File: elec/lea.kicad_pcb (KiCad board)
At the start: 2 copper layers, 76.2 x 76.2 mm, 9 parts, among them J1 Servomoteur, J2 Screw_Terminal_01x02, J3 Jack, SW1 SW_SPDT

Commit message: commit avant changement de branche
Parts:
- J2: moved to B.Cu
- moved SW1 43.6 mm to (101.6, 76.2), turned to -90 degrees
- moved C2 31.9 mm to (110.5, 76.2), turned to 180 degrees
- moved J3 22.5 mm to (120.6, 121.9), turned to 180 degrees
- moved J1 21.6 mm to (116.8, 76.2), turned to 0 degrees
- moved C1 21.1 mm to (148.7, 77.5), turned to -90 degrees
- moved A1 20.5 mm to (129.5, 77.5)
- moved J2 13.7 mm to (109.2, 68.6), turned to 90 degrees
- moved C3 7.74 mm to (121.8, 66.0), turned to 180 degrees
- moved D1 7.18 mm to (132.1, 68.6), turned to 0 degrees
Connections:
- J3 pad 1: GND -> /JCK
- J3 pad 2: /JCK -> GND
- SW1 pad 1: +9V -> unconnected-(SW1-Pad1)
- SW1 pad 3: unconnected-(SW1-Pad3) -> +9V
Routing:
- net /VIN: track 0.00 -> 66.4 mm
- net +9V: track 0.00 -> 48.8 mm
- net /JCK: track 0.00 -> 27.1 mm
- net /PWM: track 0.00 -> 17.2 mm
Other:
- outline, holes or cut-outs redrawn
- board text added: "33 × 25 mm"

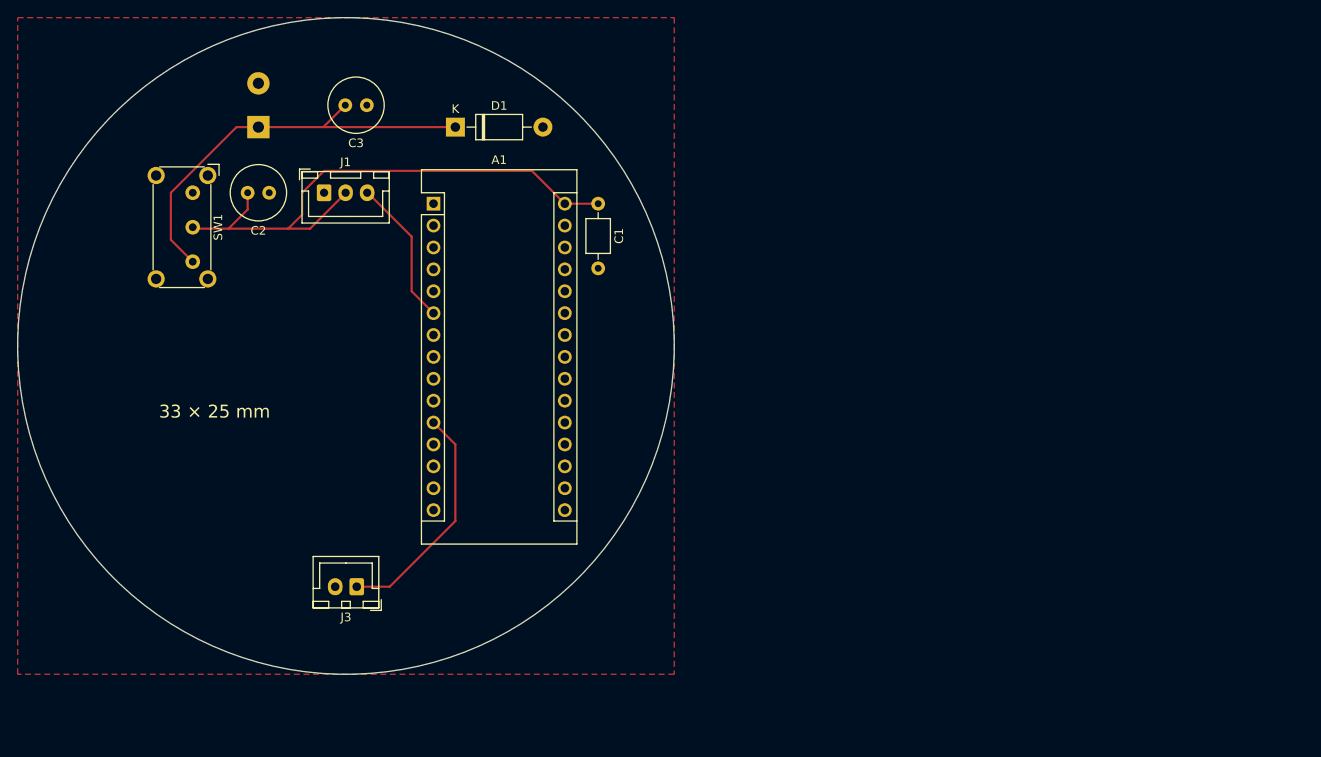
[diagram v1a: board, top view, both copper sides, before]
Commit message: Refonte complète du circuit
- réagencement des composants sur le schéma
- pcb désormais rectangulaire
- ajout du régulateur de tension et de son empreinte
- masses séparées avec possibilité de pont
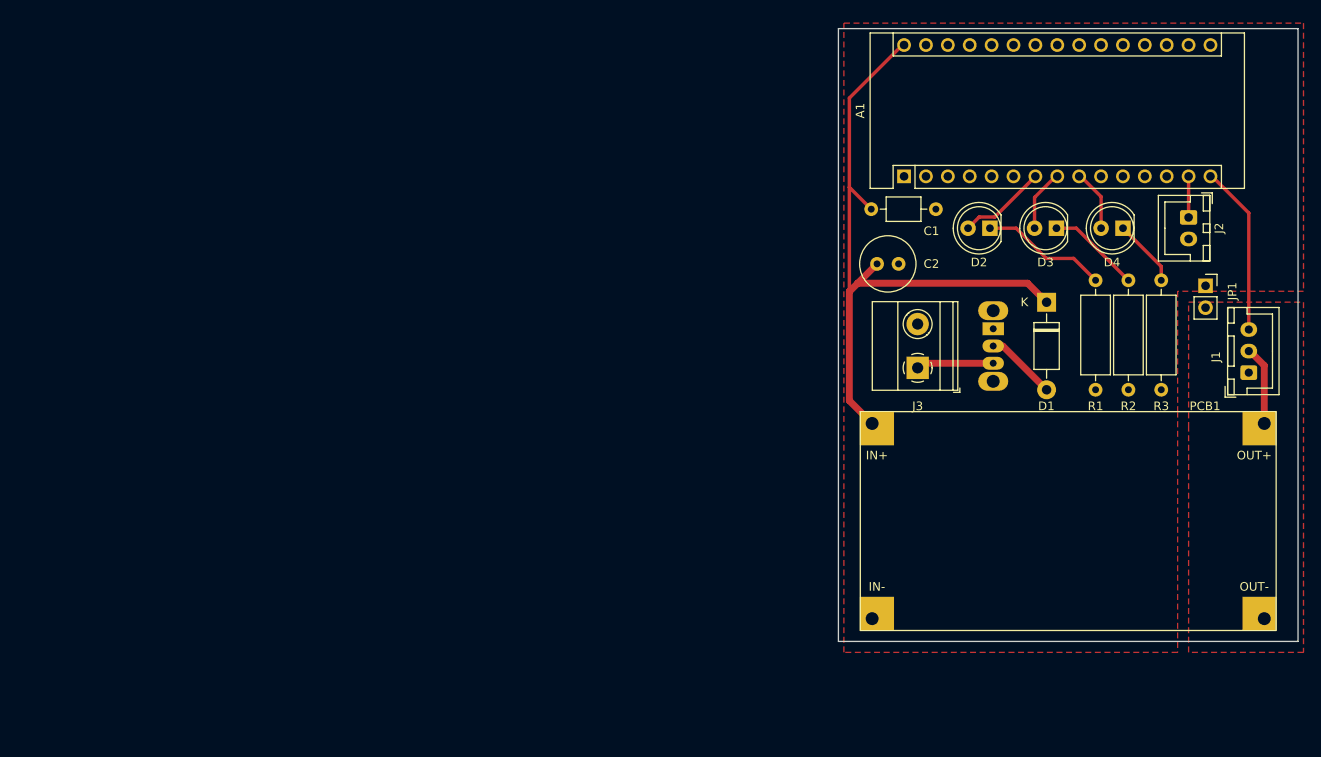
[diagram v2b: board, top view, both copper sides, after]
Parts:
- removed C3: 10uF, Capacitor_THT:C_Radial_D6.3mm_H5.0mm_P2.50mm
- added D2: LED, LED_THT:LED_D5.0mm, F.Cu at (194.1, 80.3)
- added D3: LED, LED_THT:LED_D5.0mm, F.Cu at (201.8, 80.3)
- added D4: LED, LED_THT:LED_D5.0mm, F.Cu at (209.6, 80.3)
- added JP1: Jumper_2_Open, Connector_PinSocket_2.54mm:PinSocket_1x02_P2.54mm_Vertical, F.Cu at (219.1, 87.0)
- added PCB1: abaisseur, meiVestigii:abaisseur_TOP-AERO, F.Cu at (201.9, 114.3)
- added R1: R, Resistor_THT:R_Axial_DIN0309_L9.0mm_D3.2mm_P12.70mm_Horizontal, F.Cu at (206.4, 99.1)
- added R2: R, Resistor_THT:R_Axial_DIN0309_L9.0mm_D3.2mm_P12.70mm_Horizontal, F.Cu at (210.2, 99.1)
- added R3: R, Resistor_THT:R_Axial_DIN0309_L9.0mm_D3.2mm_P12.70mm_Horizontal, F.Cu at (214.0, 99.1)
- D1: value 1N4001 -> 1N4002
- J2: value Screw_Terminal_01x02 -> Jack; footprint TerminalBlock_Phoenix:TerminalBlock_Phoenix_MKDS-1,5-2-5.08_1x02_P5.08mm_Horizontal -> Connector_JST:JST_XH_B2B-XH-A_1x02_P2.50mm_Vertical; moved to F.Cu
- J3: value Jack -> Screw_Terminal_01x02; footprint Connector_JST:JST_XH_B2B-XH-A_1x02_P2.50mm_Vertical -> TerminalBlock_Phoenix:TerminalBlock_Phoenix_MKDS-1,5-2-5.08_1x02_P5.08mm_Horizontal
- SW1: footprint Button_Switch_THT:SW_E-Switch_EG1224_SPDT_Angled -> Button_Switch_THT:SW_Slide_1P2T_CK_OS102011MS2Q; moved to B.Cu
- moved J1 109.3 mm to (224.2, 97.1), turned to 90 degrees
- moved J2 108.5 mm to (217.2, 79.1), turned to -90 degrees
- moved SW1 94.2 mm to (194.5, 92.0)
- moved C2 73.5 mm to (183.5, 84.5)
- moved D1 71.6 mm to (200.7, 88.9), turned to -90 degrees
- moved J3 69.9 mm to (185.7, 96.5), turned to 90 degrees
- moved A1 54.7 mm to (184.2, 74.3), turned to 90 degrees
- moved C1 31.7 mm to (180.3, 78.1), turned to 0 degrees
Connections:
- A1 pad 11: /JCK -> unconnected-(A1-Pad11)
- A1 pad 14: unconnected-(A1-Pad14) -> /JCK
- A1 pad 15: unconnected-(A1-Pad15) -> /PWM
- A1 pad 6: /PWM -> unconnected-(A1-Pad6)
- A1 pad 7: unconnected-(A1-Pad7) -> /D4
- A1 pad 8: unconnected-(A1-Pad8) -> /D5
- A1 pad 9: unconnected-(A1-Pad9) -> /D6
- D1 pad 1: +9V -> /VIN
- D1 pad 2: GND -> Net-(D1-Pad2)
- J1 pad 1: GND -> GND1
- J1 pad 2: /VIN -> /V1
- J2 pad 1: +9V -> /JCK
- J3 pad 1: /JCK -> +9V
- SW1 pad 2: /VIN -> Net-(D1-Pad2)
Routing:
- net +9V: track 48.8 -> 8.99 mm
- net /JCK: track 27.1 -> 4.96 mm
- net Net-(D2-Pad1): track 0.00 -> 14.8 mm
- net /VIN: track 66.4 -> 78.8 mm
- net Net-(D3-Pad1): track 0.00 -> 10.9 mm
- net /D4: track 0.00 -> 10.3 mm
- net /V1: track 0.00 -> 9.22 mm
- net Net-(D1-Pad2): track 0.00 -> 8.30 mm
- net Net-(D4-Pad1): track 0.00 -> 7.88 mm
- net /D5: track 0.00 -> 7.30 mm
- net /D6: track 0.00 -> 7.26 mm
- net /PWM: track 17.2 -> 19.8 mm
- added copper zone on F.Cu, net GND1
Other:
- board size 76.2 x 76.2 mm -> 53.3 x 71.1 mm
- board text removed: "33 × 25 mm"

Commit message: version du pcb usinable au fablab
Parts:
- A1, C1, C2, D1, D2, D3, D4, J1, J2, J3, JP1, PCB1, R1, R2, R3: moved to B.Cu
- SW1: moved to F.Cu
- moved A1 38.1 mm to (222.2, 74.3)
- moved D4 15.4 mm to (194.1, 80.3)
- moved D2 15.4 mm to (209.6, 80.3)
- moved R3 8.89 mm to (205.1, 99.1)
- moved R1 6.35 mm to (212.7, 99.1)
- moved J2 2.81 mm to (217.2, 81.9), turned to 90 degrees
- moved R2 1.27 mm to (208.9, 99.1)
- moved JP1 0.86 mm to (218.3, 87.0), turned to 180 degrees
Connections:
- A1 pad 14: /JCK -> unconnected-(A1-Pad14)
- A1 pad 15: /PWM -> unconnected-(A1-Pad15)
- A1 pad 5: unconnected-(A1-Pad5) -> /JCK
- A1 pad 6: unconnected-(A1-Pad6) -> /PWM
- J2 pad 1: /JCK -> GND
- J2 pad 2: GND -> /JCK
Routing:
- net /VIN: track 78.8 -> 134.1 mm
- net /V1: track 9.22 -> 33.5 mm
- net /PWM: track 19.8 -> 37.8 mm
- net Net-(D2-Pad1): track 14.8 -> 7.36 mm
- net Net-(D4-Pad1): track 7.88 -> 14.2 mm
- net /D6: track 7.26 -> 12.8 mm
- net /JCK: track 4.96 -> 9.42 mm
- net /D4: track 10.3 -> 6.02 mm
- net /D5: track 7.30 -> 8.16 mm
- net Net-(D3-Pad1): track 10.9 -> 10.3 mm

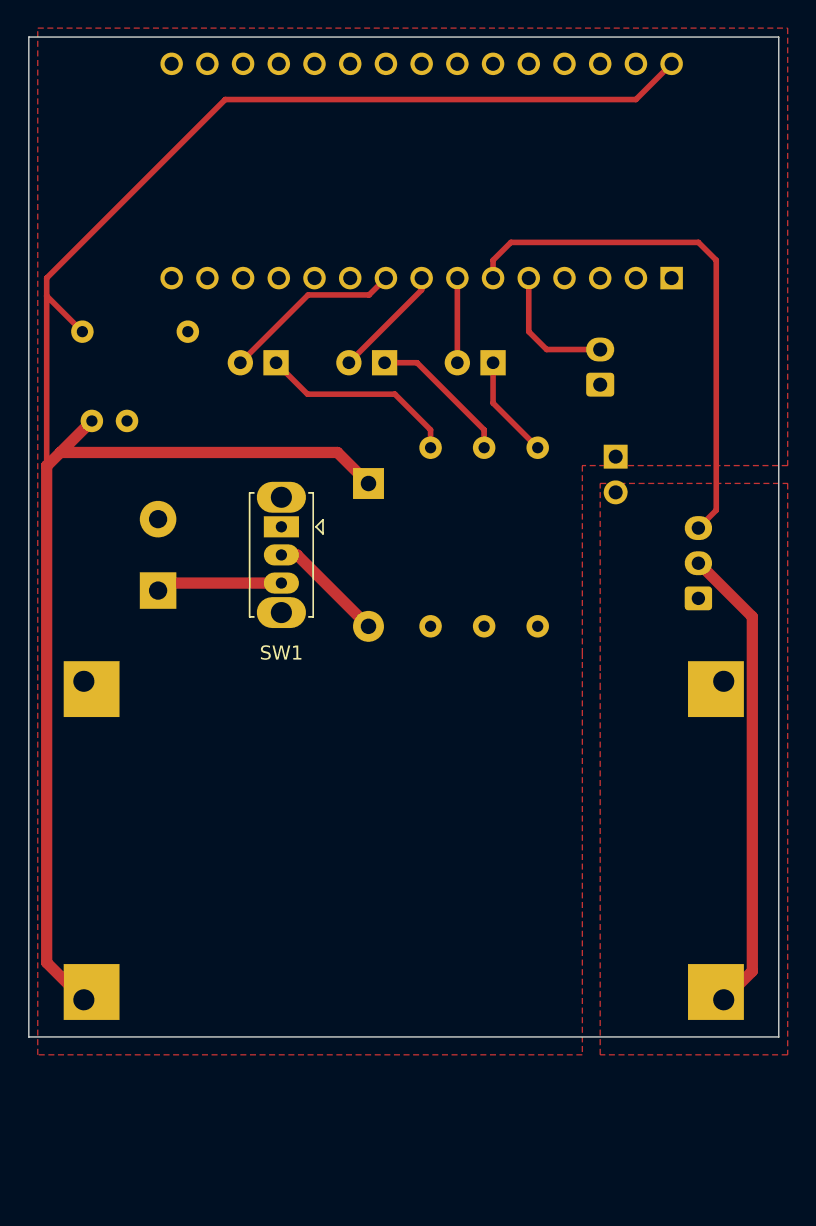
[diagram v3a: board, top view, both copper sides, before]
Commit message: switch dorénavant au format dip et nouveeau schéma pour circuit bonus
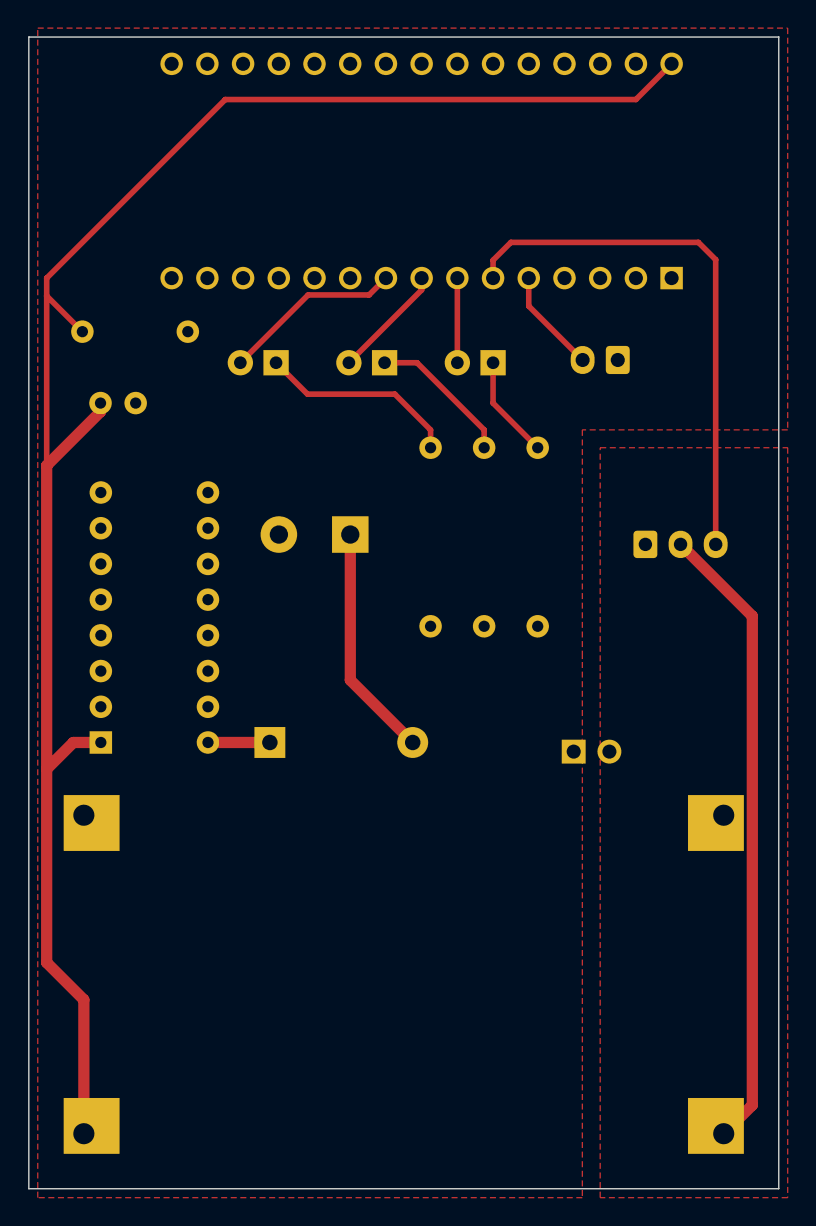
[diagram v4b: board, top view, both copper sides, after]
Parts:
- SW1: footprint Button_Switch_THT:SW_Slide_1P2T_CK_OS102011MS2Q -> Button_Switch_THT:SW_DIP_SPSTx08_Slide_9.78x22.5mm_W7.62mm_P2.54mm; moved to B.Cu
- moved JP1 21.2 mm to (215.3, 108.0), turned to -90 degrees
- moved SW1 20.0 mm to (181.7, 107.3), turned to 0 degrees
- moved D1 19.7 mm to (193.7, 107.3), turned to 0 degrees
- moved J3 14.2 mm to (199.4, 92.5), turned to 180 degrees
- moved PCB1 9.53 mm to (201.9, 123.8)
- moved J1 5.38 mm to (220.4, 93.2), turned to 0 degrees
- moved J2 2.15 mm to (218.4, 80.1), turned to 180 degrees
- moved C2 1.41 mm to (184.1, 83.2)
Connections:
- D1 pad 1: /VIN -> Net-(SW1-Pad16)
- D1 pad 2: Net-(D1-Pad2) -> +9V
- SW1 pad 1: unconnected-(SW1-Pad1) -> /VIN
- SW1 pad 2: Net-(D1-Pad2) -> unconnected-(SW1-Pad2)
- SW1 pad 3: +9V -> unconnected-(SW1-Pad3)
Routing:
- net /V1: track 33.5 -> 44.9 mm
- net Net-(D1-Pad2): track 8.30 -> 0.00 mm
- net +9V: track 8.99 -> 16.6 mm
- net /VIN: track 134.1 -> 127.0 mm
- net Net-(SW1-Pad16): track 0.00 -> 4.40 mm
- net /JCK: track 9.42 -> 7.41 mm
- net /PWM: track 37.8 -> 38.4 mm
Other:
- board size 53.3 x 71.1 mm -> 53.3 x 81.9 mm
